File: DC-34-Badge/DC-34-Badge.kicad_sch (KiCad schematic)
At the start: 1 part, among them U1 ESP32-S3-MINI-1

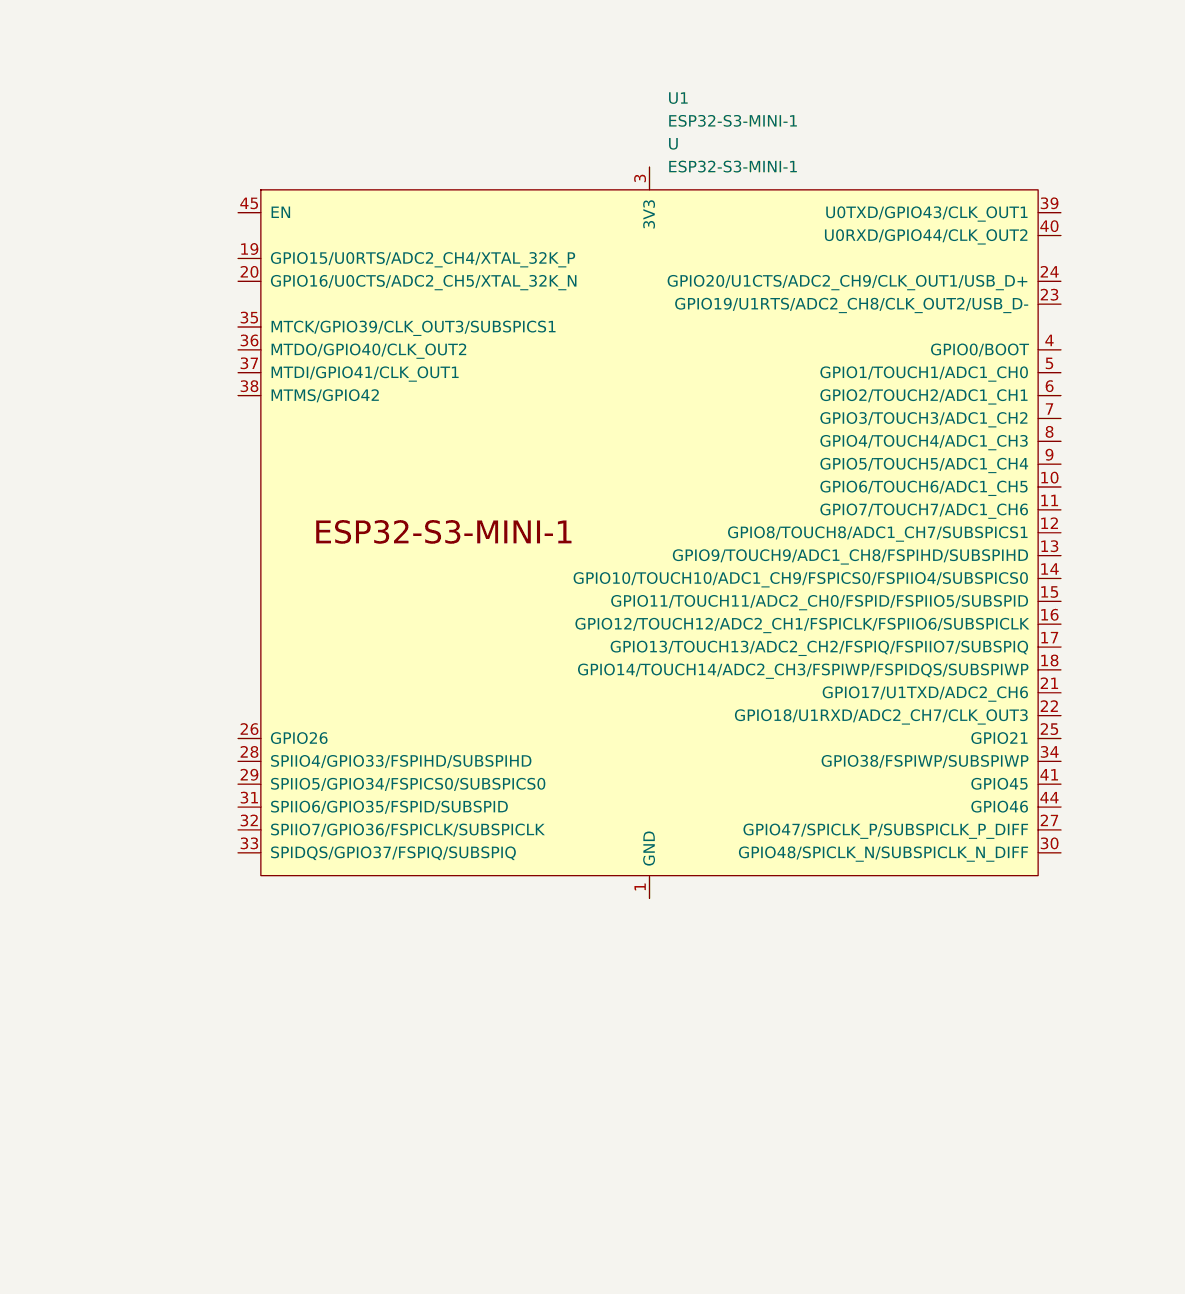
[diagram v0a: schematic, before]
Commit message: Implemented Power System
Implemented power system circuit in schematic.
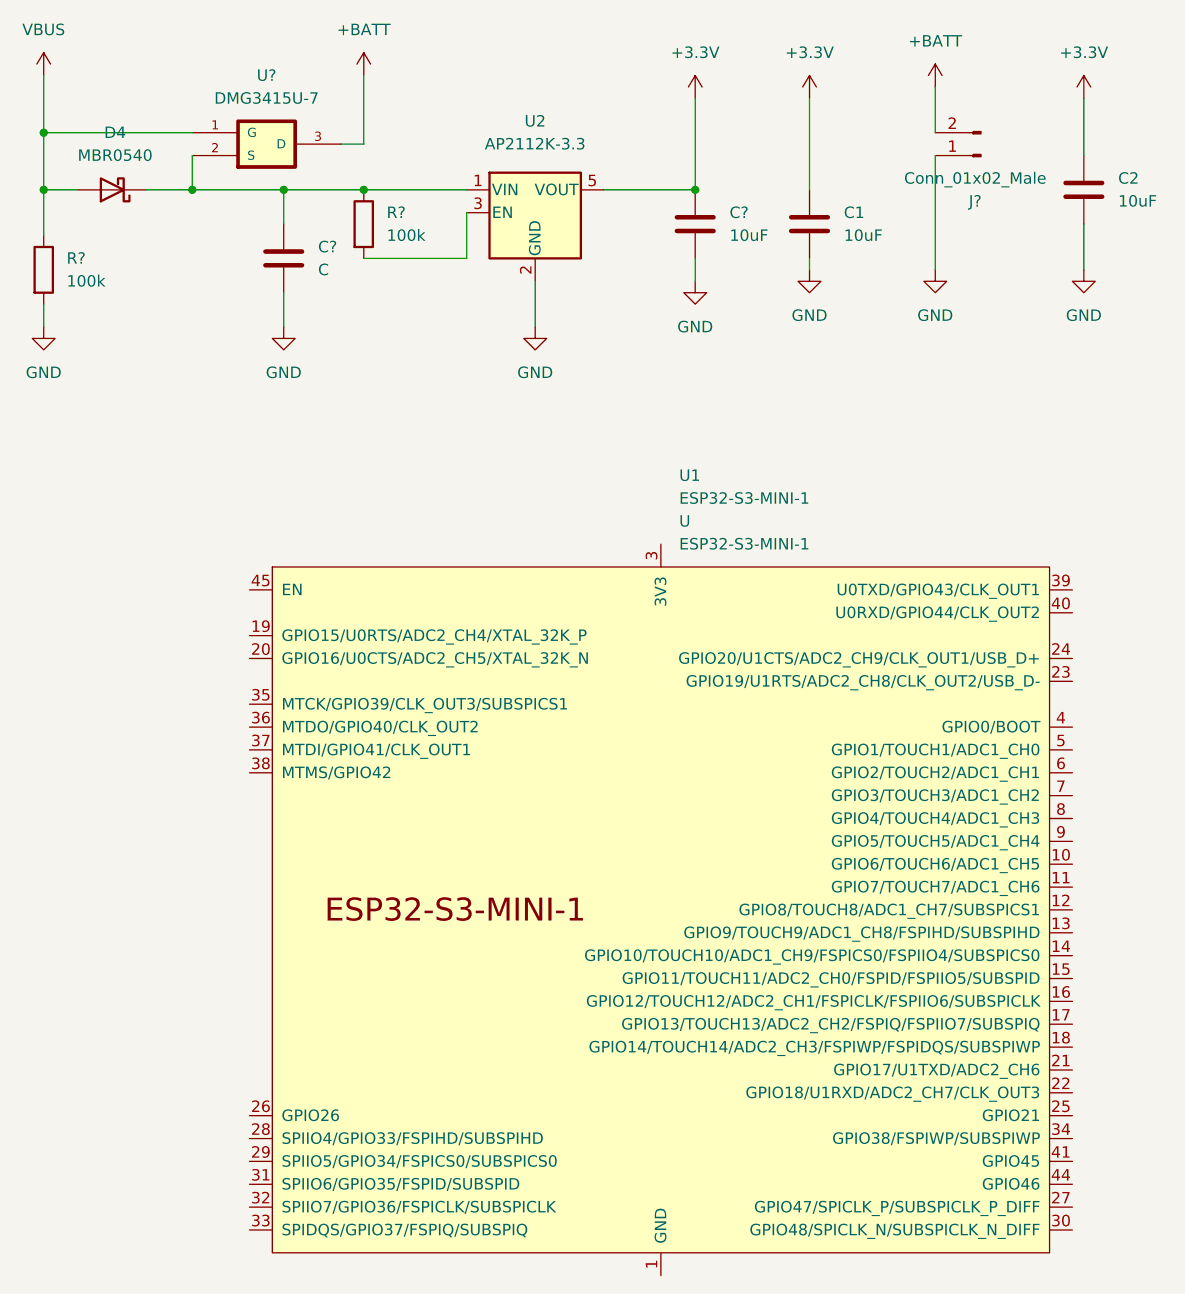
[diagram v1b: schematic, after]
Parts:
- added C1, C2, C?: 10uF, Capacitor_SMD:C_0402_1005Metric, symbol Device:C
- added C?: C, Capacitor_SMD:C_0402_1005Metric, symbol Device:C
- added D4: MBR0540, Diode_SMD:D_SOD-123, symbol Diode:MBR0540
- added J?: Conn_01x02_Male, symbol Connector:Conn_01x02_Male
- added R? (x2): 100k, Resistor_SMD:R_0402_1005Metric, symbol Device:R
- added U2: AP2112K-3.3, Package_TO_SOT_SMD:SOT-23-5, symbol Regulator_Linear:AP2112K-3.3
- added U?: DMG3415U-7, DMG3415U-7:SOT95P240X105-3N, symbol DMG3415U-7:DMG3415U-7
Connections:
- new net: C?.1, D4.1 (K), R?.1, U2.1 (VIN), U?.2 (S)
- new net: R?.2, U2.3 (EN)
- new net +3.3V: C1.1, C2.1, C?.1, U2.5 (VOUT)
- new net +BATT: J?.2 (Pin_2), U?.3 (D)
- new net GND: C1.2, C2.2, C?.2, C?.2, J?.1 (Pin_1), R?.2, U2.2 (GND)
- new net VBUS: D4.2 (A), R?.1, U?.1 (G)
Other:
- moved on the sheet: U1

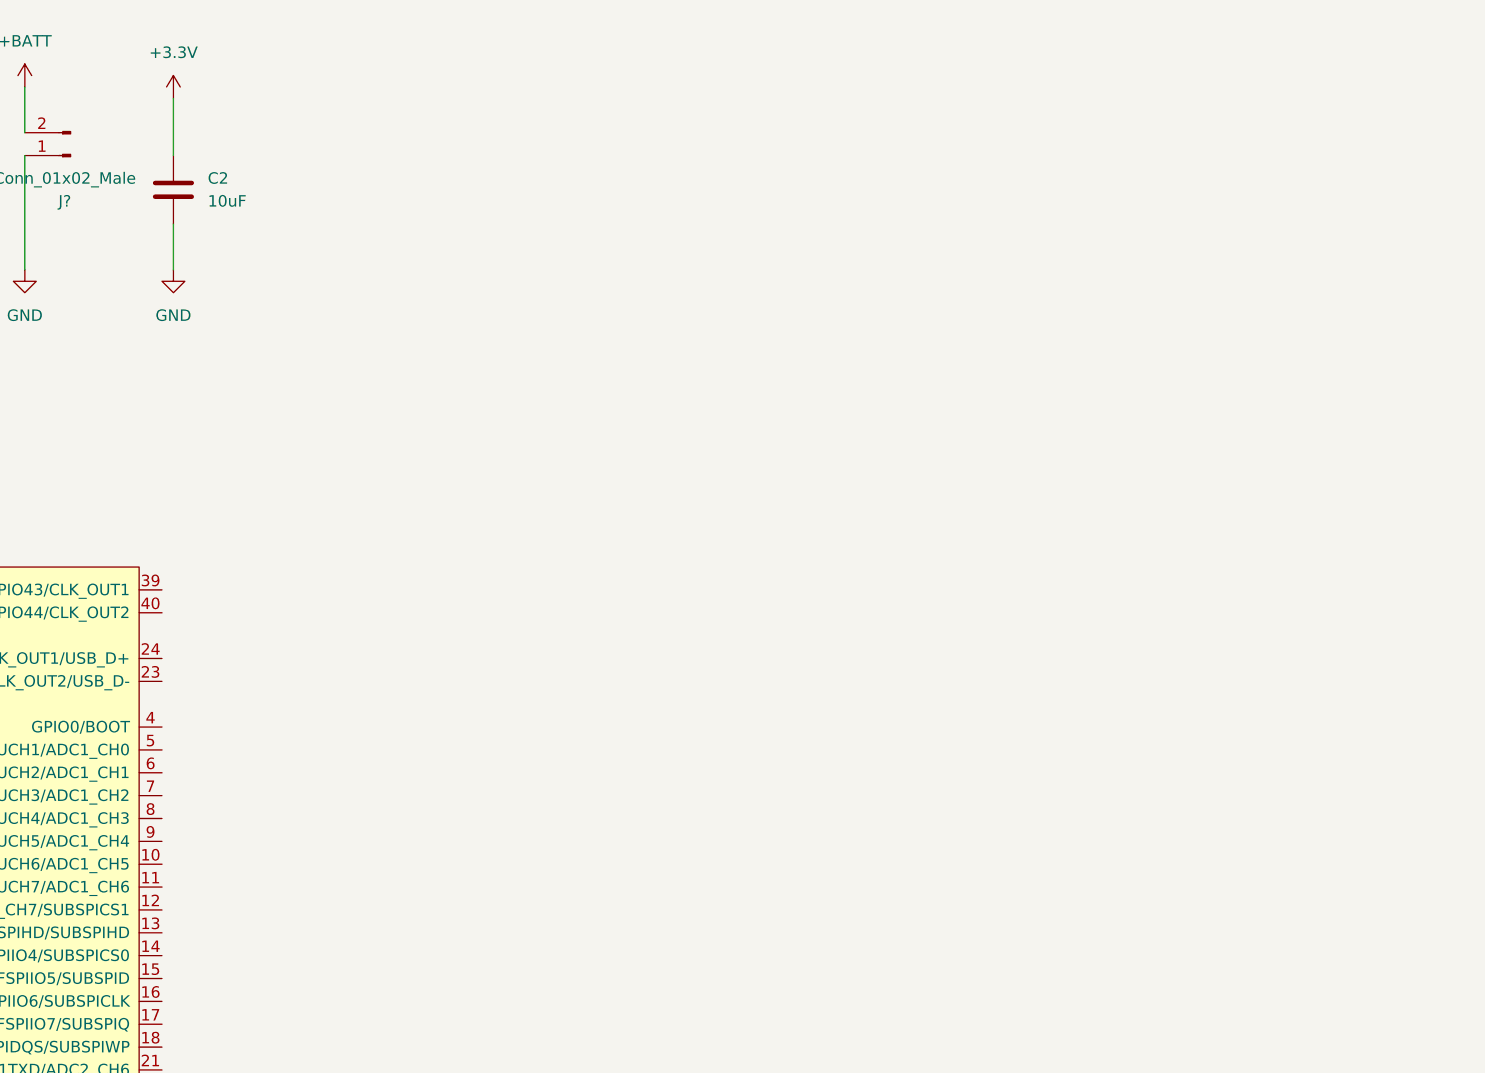
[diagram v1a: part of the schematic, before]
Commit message: Added USB
USB Bus added to design.
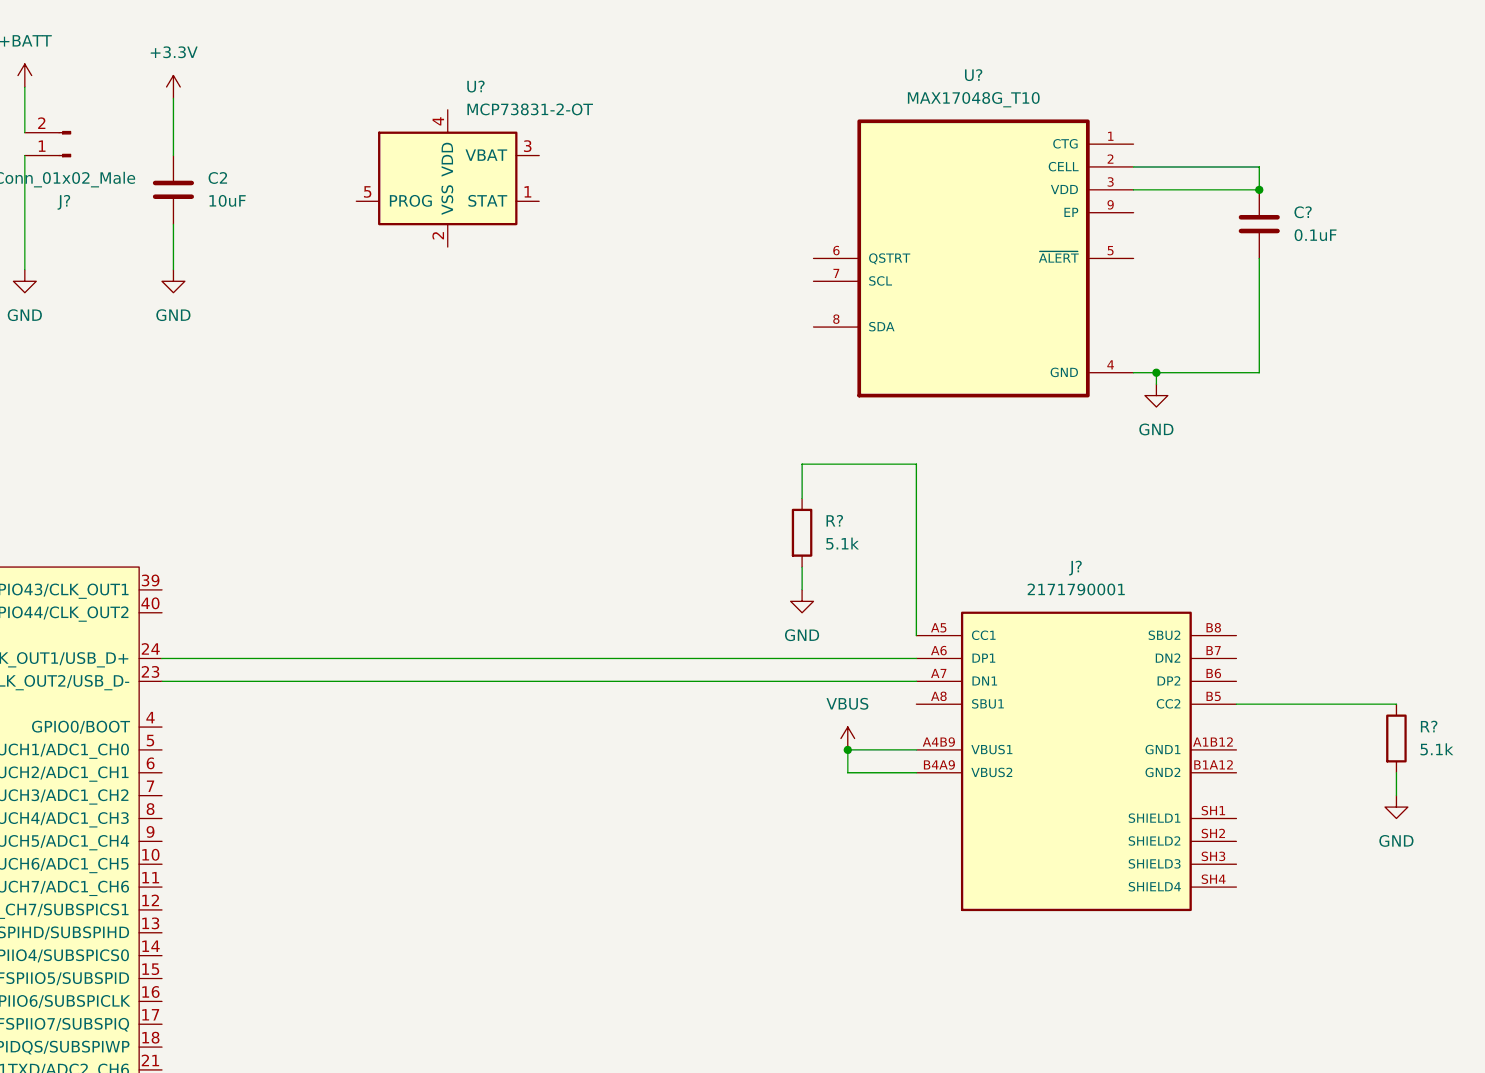
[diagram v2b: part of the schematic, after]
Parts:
- added C?: 0.1uF, Capacitor_SMD:C_0402_1005Metric, symbol Device:C
- added J?: 2171790001, 2171790001:MOLEX_2171790001, symbol 2171790001:2171790001
- added R? (x2): 5.1k, Resistor_SMD:R_0402_1005Metric, symbol Device:R
- added U?: MCP73831-2-OT, Package_TO_SOT_SMD:SOT-23-5, symbol Battery_Management:MCP73831-2-OT
- added U?: MAX17048G_T10, MAX17048G_T10:SON50P200X200X80-9N, symbol MAX17048G_T10:MAX17048G_T10
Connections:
- net GND: now also C?.2, R?.2, R?.2, U?.4 (GND)
- net VBUS: now also J?.A4B9 (VBUS1), J?.B4A9 (VBUS2)
- net at U1.23 (GPIO19/U1RTS/ADC2_CH8/CLK_OUT2/USB_D-): now also J?.A7 (DN1)
- net at U1.24 (GPIO20/U1CTS/ADC2_CH9/CLK_OUT1/USB_D+): now also J?.A6 (DP1)
- new net: C?.1, U?.2 (CELL), U?.3 (VDD)
- new net: J?.A5 (CC1), R?.1
- new net: J?.B5 (CC2), R?.1
